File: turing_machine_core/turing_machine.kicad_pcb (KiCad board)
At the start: 2 copper layers, 127 parts, among them J1 Conn_02x07_Odd_Even, Q6 55NF06, U1 74LS14, U10 74LS193, U11 AS6C1008, U12 74LS193, U13 74LS374, U14 NE555P, U15 74LS03, U16 74LS74, U17 NE555P, U19 74LS139, U2 74LS00, U20 74LS74, U21 NE555P, U22 74LS245, U23 74LS245, U24 74LS245, U25 74LS245, U26 74LS245, U27 74LS245, U28 74LS245, U29 SST39SF020, U3 74LS14, U30 74LS245, U31 74LS245, U36 74LS245, U37 D5631LA, U38 D5631LR, U4 AS6C1008, U5 74LS193, U6 74LS374, U7 74LS193, U8 74LS30, U9 AS6C1008

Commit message: PCB layout planning and further documantation work
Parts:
- removed A1: RaspberryPi_Pico, Module:RaspberryPi_Pico_Common_THT
- removed C19, C20, C21, C23, C24, C25, C26, C27: 100nF, Capacitor_THT:C_Disc_D3.8mm_W2.6mm_P2.50mm
- removed C22: 100nF, Capacitor_THT:C_Disc_D5.1mm_W3.2mm_P5.00mm
- removed D1: LED_OPERATE_R, LED_THT:LED_D5.0mm
- removed D10: LED_HEADER2, LED_THT:LED_D5.0mm
- removed D11: LED_HEADER3, LED_THT:LED_D5.0mm
- removed D12: LED_HEADER4, LED_THT:LED_D5.0mm
- removed D13: LED_HEADER5, LED_THT:LED_D5.0mm
- removed D14: LED_HEADER6, LED_THT:LED_D5.0mm
- removed D15: LED_HEADER7, LED_THT:LED_D5.0mm
- removed D16: LED_HEADER8, LED_THT:LED_D5.0mm
- removed D17: LED_HEADER9, LED_THT:LED_D5.0mm
- removed D18: LED_HEADER10, LED_THT:LED_D5.0mm
- removed D19: LED_HEADER11, LED_THT:LED_D5.0mm
- removed D2: LED_PROGRAM_R, LED_THT:LED_D5.0mm
- removed D20: LED_HEADER12, LED_THT:LED_D5.0mm
- removed D21: LED_HEADER13, LED_THT:LED_D5.0mm
- removed D22: LED_HEADER14, LED_THT:LED_D5.0mm
- removed D23: LED_HEADER15, LED_THT:LED_D5.0mm
- removed D3: LED_CLK_G, LED_THT:LED_D5.0mm
- removed D4: LED_SESR_STATE_G, LED_THT:LED_D5.0mm
- removed D5: LED_RESET_Y, LED_THT:LED_D5.0mm
- removed D6: LED_FINISH_STATE_Y, LED_THT:LED_D5.0mm
- removed D7: LED_POWER_R, LED_THT:LED_D5.0mm
- removed D8: LED_HEADER0, LED_THT:LED_D5.0mm
- removed D9: LED_HEADER1, LED_THT:LED_D5.0mm
- removed J1: Conn_02x07_Odd_Even, Connector_IDC:IDC-Header_2x07_P2.54mm_Horizontal
- removed Q6: 55NF06, Package_TO_SOT_THT:TO-220-3_Horizontal_TabDown
- removed R1, R2: 220Ω, Resistor_THT:R_Axial_DIN0207_L6.3mm_D2.5mm_P10.16mm_Horizontal
- removed R10, R19, R8: 10kΩ, Resistor_THT:R_Axial_DIN0207_L6.3mm_D2.5mm_P10.16mm_Horizontal
- removed R12, R18, R20, R3, R4, R5, R6, R7: 1kΩ, Resistor_THT:R_Axial_DIN0207_L6.3mm_D2.5mm_P10.16mm_Horizontal
- removed R21: 68Ω, Resistor_THT:R_Axial_DIN0207_L6.3mm_D2.5mm_P10.16mm_Horizontal
- removed R22, R23, R24, R25, R26, R27, R28, R29, R30, R31, R32, R33, R34, R35, R36, R37, R38, R39, R40, R41, R42, R43, R44: 330Ω, Resistor_THT:R_Axial_DIN0207_L6.3mm_D2.5mm_P10.16mm_Horizontal
- removed RN4: 1,5kΩ, Connector_PinSocket_2.54mm:PinSocket_1x08_P2.54mm_Vertical
- removed RN6: 680Ω, Connector_PinSocket_2.54mm:PinSocket_1x08_P2.54mm_Vertical
- removed the U14 at (-63.5, 101.5)
- removed the U16 at (-52.8, 113.2)
- removed the U17 at (-52.8, 101.5)
- removed U19: 74LS139, Package_DIP:DIP-16_W7.62mm
- removed U20: 74LS74, Package_DIP:DIP-14_W7.62mm
- removed U21: NE555P, Package_DIP:DIP-8_W7.62mm
- removed U26, U27, U28, U30, U31, U36: 74LS245, Package_DIP:DIP-20_W7.62mm
- removed U29: SST39SF020, Package_DIP:DIP-32_W15.24mm
- removed the U3 at (-45.5, 77.5)
- removed U37: D5631LA, Display_7Segment:DA56-11CGKWA
- removed U38: D5631LR, Display_7Segment:DA56-11CGKWA
- removed the U8 at (-34.7, 77.5)
- added C7: 100nF, Capacitor_THT:C_Disc_D3.8mm_W2.6mm_P2.50mm, F.Cu at (50.2, 101.6)
- added U13: 74LS74, Package_DIP:DIP-14_W7.62mm, F.Cu at (33.0, 33.0)
- added U6: 74LS30, Package_DIP:DIP-14_W7.62mm, F.Cu at (33.0, 101.6)
- C1, C14, C3: value 10nF -> 100nF; footprint Capacitor_THT:C_Disc_D5.1mm_W3.2mm_P5.00mm -> Capacitor_THT:C_Disc_D3.8mm_W2.6mm_P2.50mm
- C2: value 10µF -> 100nF; footprint Capacitor_THT:CP_Radial_D5.0mm_P2.00mm -> Capacitor_THT:C_Disc_D3.8mm_W2.6mm_P2.50mm
- C5: value 22nF -> 100nF; footprint Capacitor_THT:C_Disc_D5.1mm_W3.2mm_P5.00mm -> Capacitor_THT:C_Disc_D3.8mm_W2.6mm_P2.50mm
- U1: value 74LS14 -> 74LS04
- U10: renamed from U11; footprint Package_DIP:DIP-32_W15.24mm -> Package_DIP:DIP-32_W15.24mm_Socket
- U15: value 74LS03 -> 74LS245; footprint Package_DIP:DIP-14_W7.62mm -> Package_DIP:DIP-20_W7.62mm
- U3: renamed from U4; footprint Package_DIP:DIP-32_W15.24mm -> Package_DIP:DIP-32_W15.24mm_Socket
- U7: renamed from U9; footprint Package_DIP:DIP-32_W15.24mm -> Package_DIP:DIP-32_W15.24mm_Socket
- moved C18 337.5 mm to (165.1, 22.2), turned to 90 degrees
- moved C11 327.4 mm to (168.3, 99.1), turned to -90 degrees
- moved C14 316.6 mm to (147.3, 22.2), turned to 90 degrees
- moved RN3 308.9 mm to (167.6, 27.9), turned to -90 degrees
- moved C9 308.7 mm to (150.5, 99.1), turned to -90 degrees
- moved C16 301.4 mm to (129.5, 22.2), turned to 90 degrees
- moved C8 290.6 mm to (132.7, 99.1), turned to -90 degrees
- moved RN1 289.3 mm to (149.9, 27.9), turned to -90 degrees
- moved C17 286.6 mm to (111.8, 22.2), turned to 90 degrees
- moved C12 279.1 mm to (94.0, 22.2), turned to 90 degrees
- moved RN2 274.3 mm to (132.1, 27.9), turned to -90 degrees
- moved C15 273.6 mm to (114.9, 63.5), turned to -90 degrees
- moved U14 272.5 mm to (139.7, 25.4)
- moved U18 258.6 mm to (157.5, 25.4)
- moved U16 245.2 mm to (121.9, 25.4)
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- renumbered U12 to U11, U13 to U12, U22 to U14, U23 to U16, U24 to U17, U25 to U18, U6 to U4, U7 to U8, U10 to U9
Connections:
- net RPI_DATA_DIR renamed DDIR
- C1 pad 1: Net-(U14-CV) -> +5V
- C1 pad 2: COM_{1} -> GND
- C10 pad 1: LPS_{0} -> +5V
- C10 pad 2: COM_{1} -> GND
- C11 pad 1: LPS_{0} -> +5V
- C11 pad 2: COM_{1} -> GND
- C12 pad 1: LPS_{0} -> +5V
- C12 pad 2: COM_{1} -> GND
- C13 pad 1: LPS_{0} -> +5V
- C13 pad 2: COM_{1} -> GND
- C14 pad 1: Net-(U21-CV) -> +5V
- C14 pad 2: COM_{1} -> GND
- C15 pad 1: LPS_{0} -> +5V
- C15 pad 2: COM_{1} -> GND
- C16 pad 1: LPS_{0} -> +5V
- C16 pad 2: COM_{1} -> GND
- C17 pad 1: LPS_{0} -> +5V
- C17 pad 2: COM_{1} -> GND
- C18 pad 1: LPS_{0} -> +5V
- C18 pad 2: COM_{1} -> GND
- C2 pad 1: ACP_{1} -> +5V
- C2 pad 2: COM_{1} -> GND
- C3 pad 1: Net-(U17-CV) -> +5V
- C3 pad 2: COM_{1} -> GND
- C4 pad 1: Net-(C4-Pad1) -> +5V
- C4 pad 2: COM_{1} -> GND
- C5 pad 1: Net-(U17-THR) -> +5V
- C5 pad 2: COM_{1} -> GND
- C6 pad 1: Net-(C6-Pad1) -> +5V
- C6 pad 2: COM_{1} -> GND
- C8 pad 1: Net-(C8-Pad1) -> +5V
- C8 pad 2: COM_{1} -> GND
- C9 pad 1: LPS_{0} -> +5V
- C9 pad 2: COM_{1} -> GND
- RN1 pad 1: COM_{1} -> GND
- RN2 pad 1: COM_{1} -> GND
- RN3 pad 1: LPS_{0} -> +5V
- RN3 pad 8: DIR -> /Control signal buffers/QR_~{OE}
- RN3 pad 9: unconnected-(RN3-R8-Pad9) -> DIR
- U1 pad 1: Net-(C4-Pad1) -> Net-(U1-Pad1)
- U1 pad 10: /RaspberryPI and power/REPROGRAM -> Net-(U13A-C)
- U1 pad 11: Net-(C8-Pad1) -> Net-(U1-Pad11)
- U1 pad 12: /RESET -> ~{OPERATE}
- U1 pad 13: ~{RESET} -> ~{PROGRAM}
- U1 pad 14: LPS_{0} -> +5V
- U1 pad 2: /Clock and Execution State/MAN_CLK -> /HP_EN_CLK
- U1 pad 3: Net-(U1-Pad3) -> DIR
- U1 pad 5: ~{PROGRAM} -> HP_EN
- U1 pad 6: ~{OPERATE} -> SR_WR
- U1 pad 7: COM_{1} -> GND
- U1 pad 8: Net-(U1-Pad3) -> /RESET
- U1 pad 9: Net-(C6-Pad1) -> ~{RESET}
- U10 pad 16: COM_{1} -> GND
- U10 pad 2: LPS_{0} -> +5V
- U10 pad 22: COM_{1} -> GND
- U10 pad 30: LPS_{0} -> +5V
- U10 pad 31: LPS_{0} -> +5V
- U10 pad 32: LPS_{0} -> +5V
- U11 pad 1: LPS_{0} -> +5V
- U11 pad 10: LPS_{0} -> +5V
- U11 pad 11: LPS_{0} -> +5V
- U11 pad 15: LPS_{0} -> +5V
- U11 pad 16: LPS_{0} -> +5V
- U11 pad 8: COM_{1} -> GND
- U11 pad 9: LPS_{0} -> +5V
- U12 pad 1: COM_{1} -> GND
- U12 pad 10: COM_{1} -> GND
- U12 pad 20: LPS_{0} -> +5V
- U14 pad 10: COM_{1} -> GND
- U14 pad 2: RD_{0} -> D_{0}
- U14 pad 20: LPS_{0} -> +5V
- U14 pad 3: RD_{1} -> D_{1}
- U14 pad 4: RD_{2} -> D_{2}
- U14 pad 5: RD_{3} -> D_{3}
- U14 pad 6: RD_{4} -> D_{4}
- U14 pad 7: RD_{5} -> D_{5}
- U14 pad 8: RD_{6} -> D_{6}
- U14 pad 9: RD_{7} -> D_{7}
- U15 pad 1: Net-(U1-Pad3) -> +5V
- U15 pad 10: /Clock and Execution State/COMBINED_CLK -> GND
- U15 pad 11: CLK -> D_{7}
- U15 pad 12: RPI_CLK -> D_{6}
- U15 pad 13: ~{OPERATE} -> D_{5}
- U15 pad 14: LPS_{0} -> D_{4}
- U15 pad 2: /Clock and Execution State/MAN_CLK -> QR_{0}
- U15 pad 3: /Clock and Execution State/COMBINED_CLK -> QR_{1}
- U15 pad 4: Net-(U1-Pad4) -> QR_{2}
- U15 pad 5: /Clock and Execution State/AUTO_CLK -> QR_{3}
- U15 pad 6: /Clock and Execution State/COMBINED_CLK -> QR_{4}
- U15 pad 7: COM_{1} -> QR_{5}
- U15 pad 8: CLK -> QR_{6}
- U15 pad 9: ~{PROGRAM} -> QR_{7}
- U16 pad 10: COM_{1} -> GND
- U16 pad 2: RD_{0} -> D_{0}
- U16 pad 20: LPS_{0} -> +5V
- U16 pad 3: RD_{1} -> D_{1}
- U16 pad 4: RD_{2} -> D_{2}
- U16 pad 5: RD_{3} -> D_{3}
- U16 pad 6: RD_{4} -> D_{4}
- U16 pad 7: RD_{5} -> D_{5}
- U16 pad 8: RD_{6} -> D_{6}
- U16 pad 9: RD_{7} -> D_{7}
- U17 pad 1: LPS_{0} -> +5V
- U17 pad 10: COM_{1} -> GND
- U17 pad 2: SESR_STATE -> HP_EN
- U17 pad 20: LPS_{0} -> +5V
- U17 pad 7: COM_{1} -> GND
- U17 pad 8: COM_{1} -> GND
- U17 pad 9: COM_{1} -> GND
- U18 pad 1: LPS_{0} -> +5V
- U18 pad 10: COM_{1} -> GND
- U18 pad 12: unconnected-(U25-B6-Pad12) -> /Control signal buffers/QR_~{OE}
- U18 pad 2: RD_{8} -> T_~{OE}_E
- U18 pad 20: LPS_{0} -> +5V
- U18 pad 3: RD_{9} -> T_~{WE}_E
- U18 pad 4: RD_{10} -> SYT_~{OE}_E
- U18 pad 5: RD_{11} -> SYT_~{WE}_E
- U18 pad 6: RD_{12} -> STT_~{OE}_E
- U18 pad 7: RD_{13} -> STT_~{WE}_E
- U18 pad 8: RD_{14} -> QR_~{OE}_E
- U18 pad 9: RD_{15} -> +5V
- U2 pad 1: CLK -> DIR
- U2 pad 10: /TI_EN_CLK -> HP_EN
- U2 pad 11: /DIR_DOWN -> Net-(U1-Pad11)
- U2 pad 12: /TI_EN_CLK -> ~{FINISH_STATE}
- U2 pad 13: Net-(U2-Pad13) -> CLK
- U2 pad 14: LPS_{0} -> +5V
- U2 pad 2: SESR_STATE -> /HP_EN_CLK
- U2 pad 3: Net-(U2-Pad3) -> /DIR_UP
- U2 pad 4: unconnected-(U2-Pad4) -> /HP_EN_CLK
- U2 pad 5: unconnected-(U2-Pad5) -> Net-(U1-Pad4)
- U2 pad 6: unconnected-(U2-Pad6) -> /DIR_DOWN
- U2 pad 7: COM_{1} -> GND
- U2 pad 8: /DIR_UP -> Net-(U1-Pad1)
- U2 pad 9: DIR -> CLK
- U3 pad 16: COM_{1} -> GND
- U3 pad 2: LPS_{0} -> +5V
- U3 pad 22: COM_{1} -> GND
- U3 pad 30: LPS_{0} -> +5V
- U3 pad 32: LPS_{0} -> +5V
- U4 pad 1: COM_{1} -> GND
- U4 pad 10: COM_{1} -> GND
- U4 pad 11: SESR_STATE -> HP_EN
- U4 pad 18: LPS_{0} -> +5V
- U4 pad 20: LPS_{0} -> +5V
- U5 pad 1: LPS_{0} -> +5V
- U5 pad 10: LPS_{0} -> +5V
- U5 pad 11: LPS_{0} -> +5V
- U5 pad 15: LPS_{0} -> +5V
- U5 pad 16: LPS_{0} -> +5V
- U5 pad 8: COM_{1} -> GND
- U5 pad 9: LPS_{0} -> +5V
- U7 pad 16: COM_{1} -> GND
- U7 pad 2: LPS_{0} -> +5V
- U7 pad 22: COM_{1} -> GND
- U7 pad 30: LPS_{0} -> +5V
- U7 pad 31: LPS_{0} -> +5V
- U7 pad 32: LPS_{0} -> +5V
- U8 pad 1: LPS_{0} -> +5V
- U8 pad 10: LPS_{0} -> +5V
- U8 pad 11: LPS_{0} -> +5V
- U8 pad 15: LPS_{0} -> +5V
- U8 pad 16: LPS_{0} -> +5V
- U8 pad 8: COM_{1} -> GND
- U8 pad 9: LPS_{0} -> +5V
- U9 pad 1: LPS_{0} -> +5V
- U9 pad 10: LPS_{0} -> +5V
- U9 pad 11: LPS_{0} -> +5V
- U9 pad 15: LPS_{0} -> +5V
- U9 pad 16: LPS_{0} -> +5V
- U9 pad 8: COM_{1} -> GND
- U9 pad 9: LPS_{0} -> +5V
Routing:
- net GND: track 0.00 -> 998.5 mm, vias 0 -> 16
- net +5V: track 0.00 -> 610.9 mm, vias 0 -> 2
- net QR_{1}: track 0.00 -> 226.9 mm, vias 0 -> 8
- net QR_{2}: track 0.00 -> 221.1 mm, vias 0 -> 8
- net QR_{0}: track 0.00 -> 215.5 mm, vias 0 -> 6
- net QR_{3}: track 0.00 -> 213.9 mm, vias 0 -> 8
- net S_{0}: track 0.00 -> 195.9 mm, vias 0 -> 3
- net S_{1}: track 0.00 -> 192.8 mm, vias 0 -> 4
- net S_{2}: track 0.00 -> 192.0 mm, vias 0 -> 4
- net QR_{6}: track 0.00 -> 187.6 mm, vias 0 -> 6
- net QR_{5}: track 0.00 -> 185.1 mm, vias 0 -> 7
- net QR_{4}: track 0.00 -> 180.3 mm, vias 0 -> 6
- net QR_{7}: track 0.00 -> 175.6 mm, vias 0 -> 3
- net S_{4}: track 0.00 -> 158.2 mm, vias 0 -> 6
- net S_{3}: track 0.00 -> 158.2 mm, vias 0 -> 4
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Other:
- board outline added: 152.4 x 110.5 mm
- board text added: "(STATE REGISTER)"
- board text added: "(STATE TRANSLATOR)"
- board text added: "(SYMBOL REGISTER)"
- board text added: "(SYMBOL TRANSLATOR)"
- board text added: "(TAPE)"
- board text added: "1"
- board text added: "2"
- board text added: "3"
- board text added: "4"
- board text added: "5"
- board text added: "6"
- board text added: "7"
- board text added: "8"
- board text added: "A"
- board text added: "B"
- board text added: "C"

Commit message: finished PCB planning
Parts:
- added D1: Power LED, LED_THT:LED_D5.0mm, F.Cu at (55.9, 21.6)
- added R1: 1kΩ, Resistor_THT:R_Axial_DIN0207_L6.3mm_D2.5mm_P10.16mm_Horizontal, F.Cu at (41.9, 21.6)
- added REF**: KiCad-Logo2_8mm_SilkScreen, Symbol:KiCad-Logo2_8mm_SilkScreen, B.Cu at (137.8, 59.7)
- added REF**: OSHW-Logo_11.4x12mm_SilkScreen, Symbol:OSHW-Logo_11.4x12mm_SilkScreen, B.Cu at (157.5, 59.7)
- moved C2 4.50 mm to (61.6, 33.0)
- moved C1 4.49 mm to (79.4, 33.0)
- moved C13 4.49 mm to (43.8, 33.0)
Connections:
- U13 pad 10: unconnected-(U13B-~{S}-Pad10) -> +5V
- U13 pad 11: unconnected-(U13B-C-Pad11) -> GND
- U13 pad 12: unconnected-(U13B-D-Pad12) -> GND
- U13 pad 13: unconnected-(U13B-~{R}-Pad13) -> GND
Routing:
- net STT_~{OE}: track 2.54 -> 277.3 mm, vias 0 -> 6
- net SYT_~{OE}: track 2.54 -> 253.7 mm, vias 0 -> 11
- net DIR_B: track 2.54 -> 224.3 mm, vias 0 -> 10
- net SYT_~{WE}: track 2.54 -> 177.0 mm, vias 0 -> 4
- net HP_EN: track 0.00 -> 166.3 mm, vias 0 -> 7
- net STT_~{WE}: track 2.54 -> 166.2 mm, vias 0 -> 2
- net DIR: track 0.00 -> 161.0 mm, vias 0 -> 9
- net Q_{0}: track 2.54 -> 146.6 mm, vias 0 -> 3
- net Q_{1}: track 2.54 -> 142.6 mm, vias 0 -> 4
- net T_~{OE}: track 2.54 -> 132.4 mm, vias 0 -> 6
- net Q_{2}: track 2.54 -> 130.8 mm, vias 0 -> 4
- net T_~{WE}: track 2.54 -> 129.5 mm, vias 0 -> 7
- net Q_{7}: track 2.54 -> 117.4 mm, vias 0 -> 3
- net Q_{6}: track 2.54 -> 116.3 mm, vias 0 -> 4
- net Q_{3}: track 2.54 -> 110.2 mm, vias 0 -> 4
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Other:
- board text added: "02.2026"
- board text added: "Fizyczna implementacja maszyny Turinga"
- board text added: "Paweł Szymańki"
- board text added: "Paweł Szymański 02.2026"
- board text added: "Power"
- board text added: "Tura"

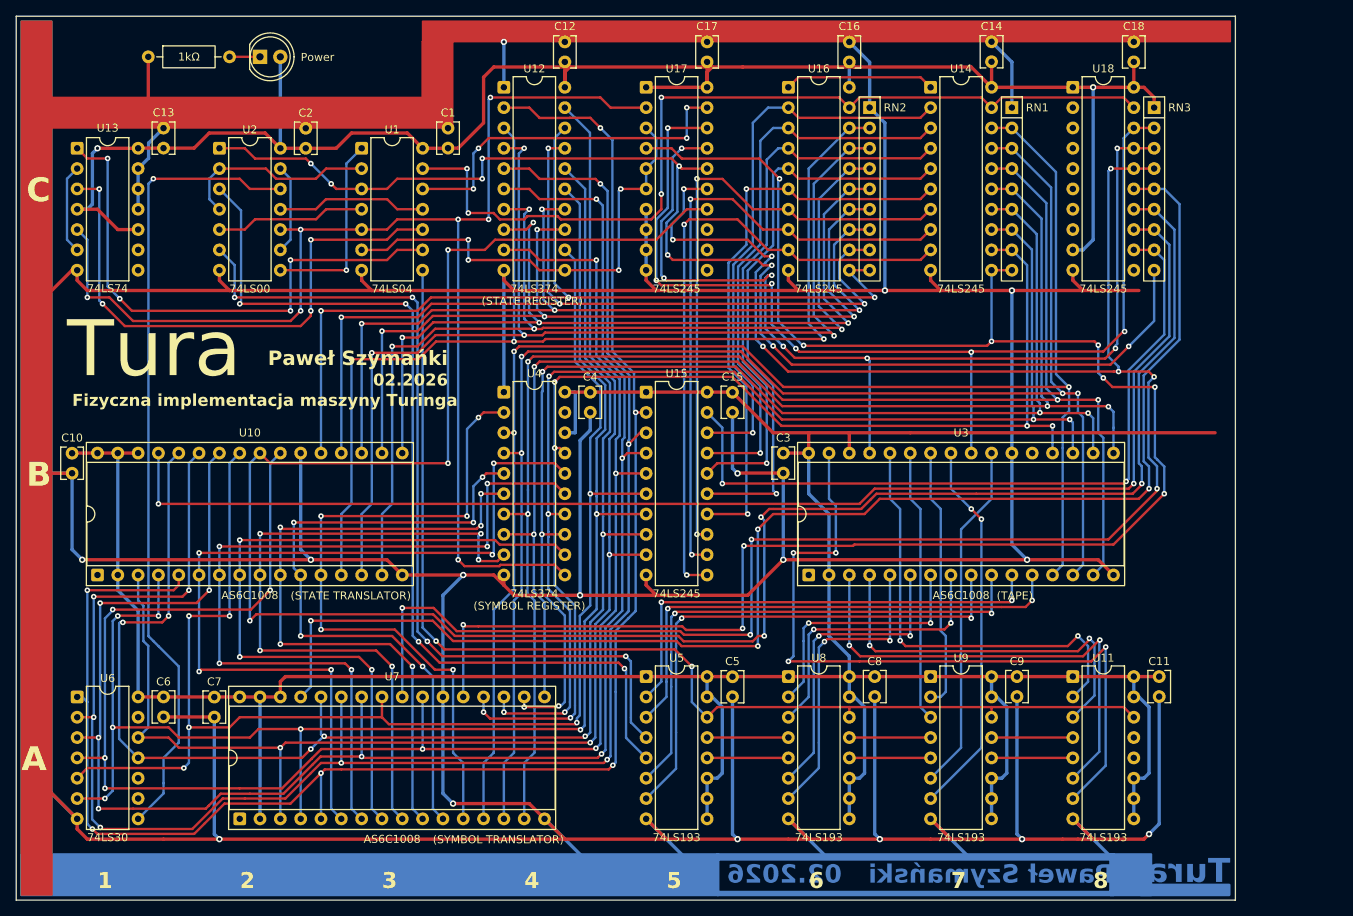
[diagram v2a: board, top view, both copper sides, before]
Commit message: adjusted PCB design for schematic fixes
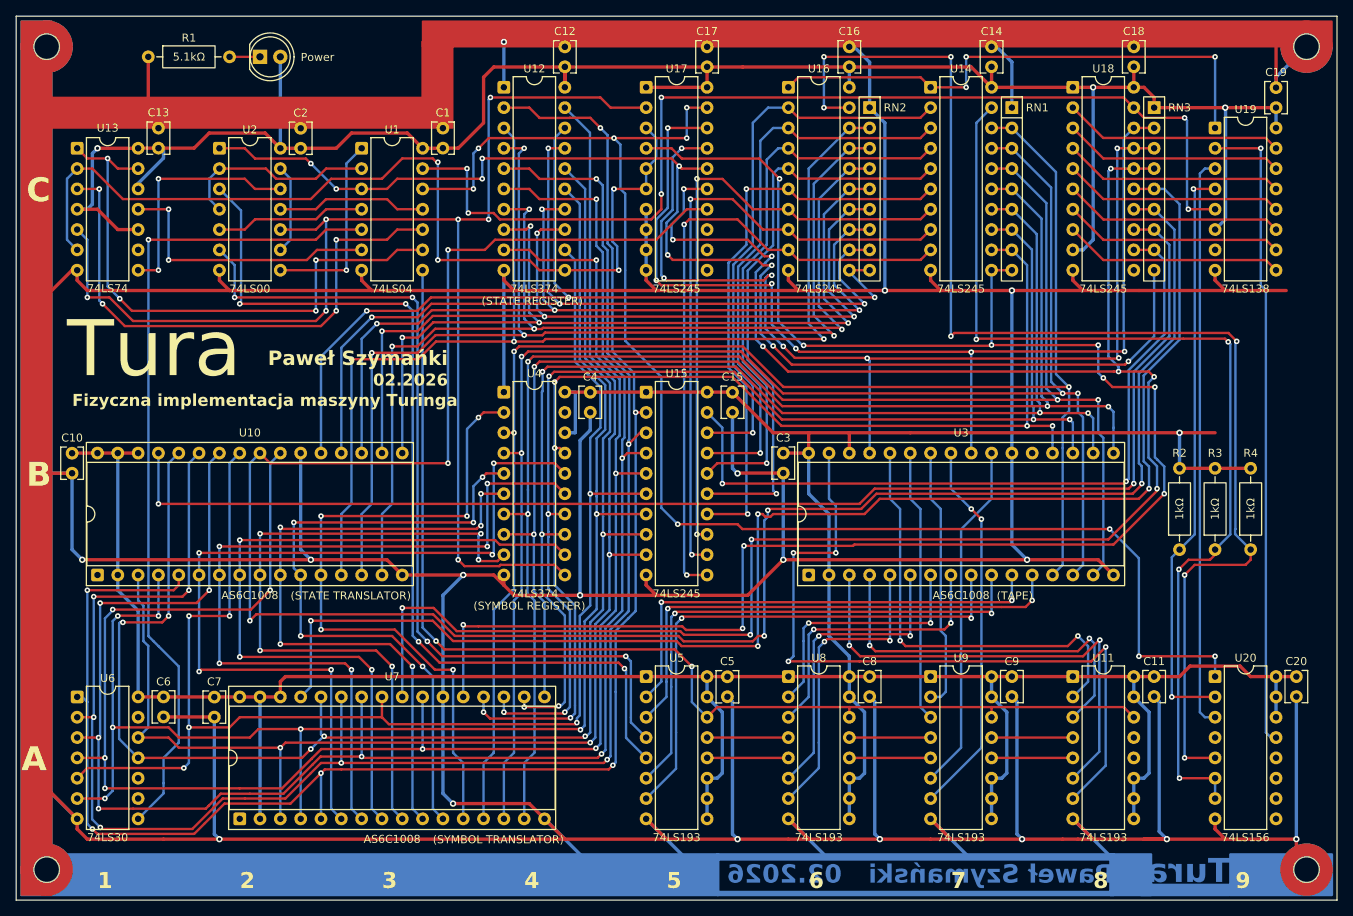
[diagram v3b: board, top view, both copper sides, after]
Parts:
- removed the REF** at (137.8, 59.7)
- removed the REF** at (157.5, 59.7)
- added C19: 100nF, Capacitor_THT:C_Disc_D3.8mm_W2.6mm_P2.50mm, F.Cu at (182.9, 27.9)
- added C20: 100nF, Capacitor_THT:C_Disc_D3.8mm_W2.6mm_P2.50mm, F.Cu at (185.4, 99.1)
- added R2: 1kΩ, Resistor_THT:R_Axial_DIN0207_L6.3mm_D2.5mm_P10.16mm_Horizontal, F.Cu at (170.8, 83.2)
- added R3: 1kΩ, Resistor_THT:R_Axial_DIN0207_L6.3mm_D2.5mm_P10.16mm_Horizontal, F.Cu at (175.3, 83.2)
- added R4: 1kΩ, Resistor_THT:R_Axial_DIN0207_L6.3mm_D2.5mm_P10.16mm_Horizontal, F.Cu at (179.7, 83.2)
- added REF**: MountingHole_3.2mm_M3, MountingHole:MountingHole_3.2mm_M3, F.Cu at (29.2, 123.2)
- added REF**: MountingHole_3.2mm_M3, MountingHole:MountingHole_3.2mm_M3, F.Cu at (186.7, 123.2)
- added REF**: MountingHole_3.2mm_M3, MountingHole:MountingHole_3.2mm_M3, F.Cu at (186.7, 20.3)
- added REF**: MountingHole_3.2mm_M3, MountingHole:MountingHole_3.2mm_M3, F.Cu at (29.2, 20.3)
- added U19: 74LS138, Package_DIP:DIP-16_W7.62mm, F.Cu at (175.3, 30.5)
- added U20: 74LS156, Package_DIP:DIP-16_W7.62mm, F.Cu at (175.3, 99.1)
- R1: value 1kΩ -> 5.1kΩ
- moved C11 0.64 mm to (167.6, 99.1)
- moved C1 0.64 mm to (78.7, 33.0)
- moved C5 0.64 mm to (114.3, 99.1)
- moved C14 0.64 mm to (147.3, 22.8)
- moved C13 0.63 mm to (43.2, 33.0)
- moved C2 0.63 mm to (61.0, 33.0)
- moved C8 0.63 mm to (132.1, 99.1)
- moved C9 0.63 mm to (149.9, 99.1)
- moved C12 0.61 mm to (94.0, 22.8)
- moved C16 0.61 mm to (129.5, 22.8)
- moved C17 0.61 mm to (111.8, 22.8)
- moved C18 0.61 mm to (165.1, 22.8)
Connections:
- U1 pad 5: HP_EN -> ~{FINISH_STATE}
- U1 pad 6: SR_WR -> Net-(U13B-C)
- U13 pad 11: GND -> Net-(U13B-C)
- U13 pad 12: GND -> +5V
- U13 pad 13: GND -> ~{RESET}
- U13 pad 2: Net-(U13A-D) -> SR_WR
- U13 pad 6: Net-(U13A-D) -> SR_WR
- U13 pad 8: unconnected-(U13B-~{Q}-Pad8) -> /Execution State & Power/CLK_EN
- U14 pad 19: ~{PROGRAM} -> ~{SYMB_BUF}
- U16 pad 19: ~{PROGRAM} -> ~{STAT_BUF}
- U2 pad 12: ~{FINISH_STATE} -> /Execution State & Power/CLK_EN
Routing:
- net ~{STAT_BUF}: track 0.00 -> 160.6 mm, vias 0 -> 7
- net ~{OPERATE}: track 44.6 -> 179.9 mm, vias 4 -> 9
- net ~{SYMB_BUF}: track 0.00 -> 127.4 mm, vias 0 -> 4
- net CS_{0}: track 0.00 -> 80.5 mm, vias 0 -> 1
- net ~{DT}: track 0.00 -> 72.9 mm, vias 0 -> 2
- net CS_{1}: track 0.00 -> 71.6 mm
- net +5V: track 622.5 -> 693.9 mm, vias 2 -> 4
- net GND: track 1009.7 -> 1076.7 mm, vias 16 -> 17
- net SR_WR: track 57.8 -> 118.9 mm
- net DDIR: track 18.8 -> 67.1 mm, vias 0 -> 3
- net Net-(U13B-C): track 0.00 -> 34.8 mm, vias 0 -> 2
- net /Execution State & Power/CLK_EN: track 0.00 -> 29.7 mm, vias 0 -> 2
- net T_~{WE}_E: track 0.00 -> 27.5 mm
- net T_~{OE}_E: track 0.00 -> 27.5 mm
- net SYT_~{WE}_E: track 0.00 -> 27.5 mm
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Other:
- board size 152.4 x 110.5 mm -> 165.1 x 110.5 mm
- board text added: "9"

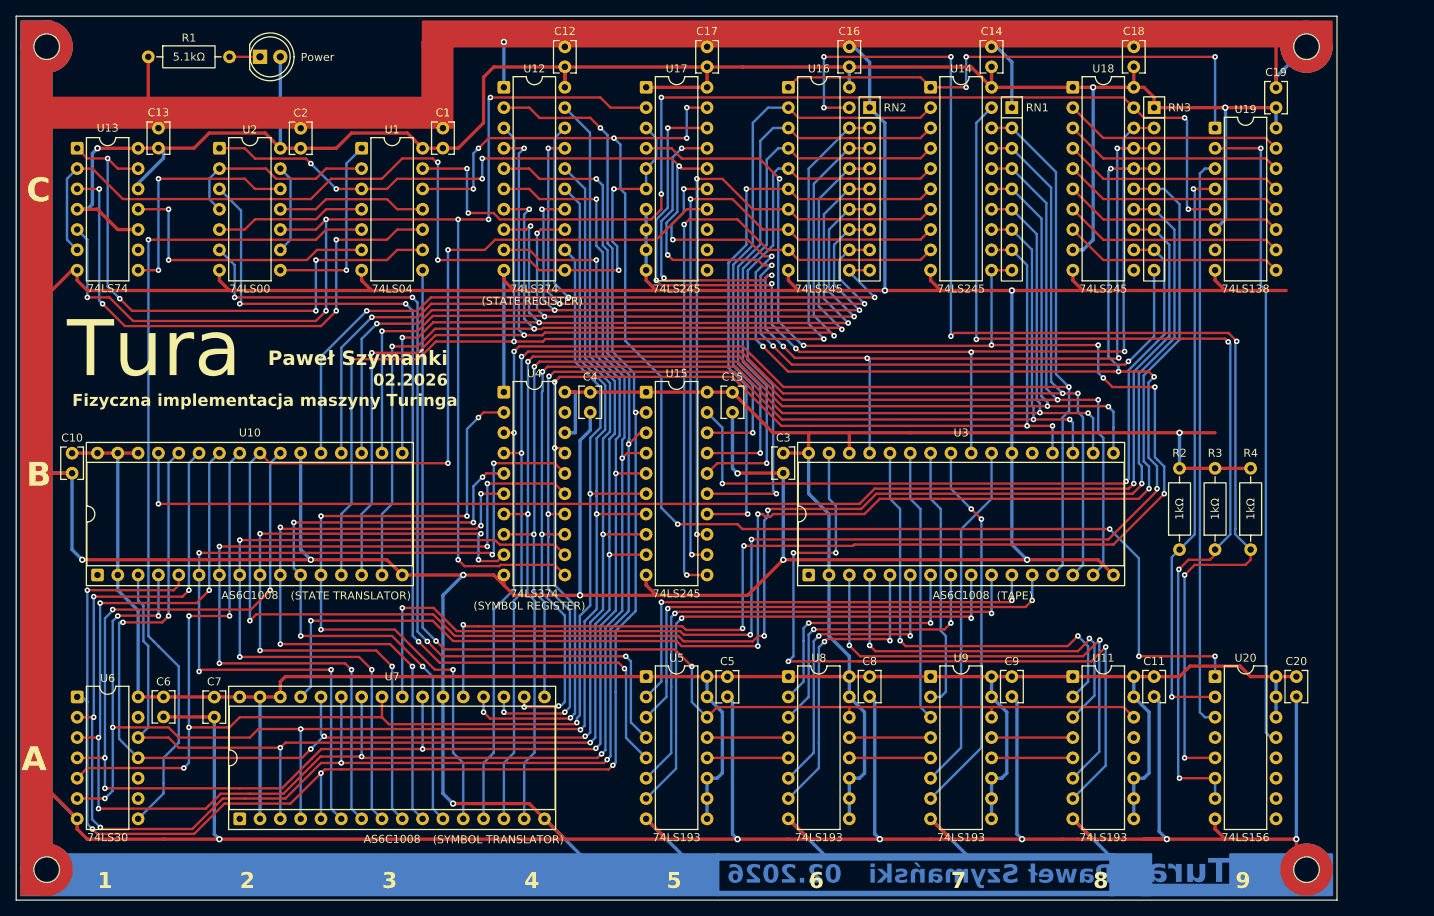
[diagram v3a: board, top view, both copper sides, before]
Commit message: added edge connector to PCB
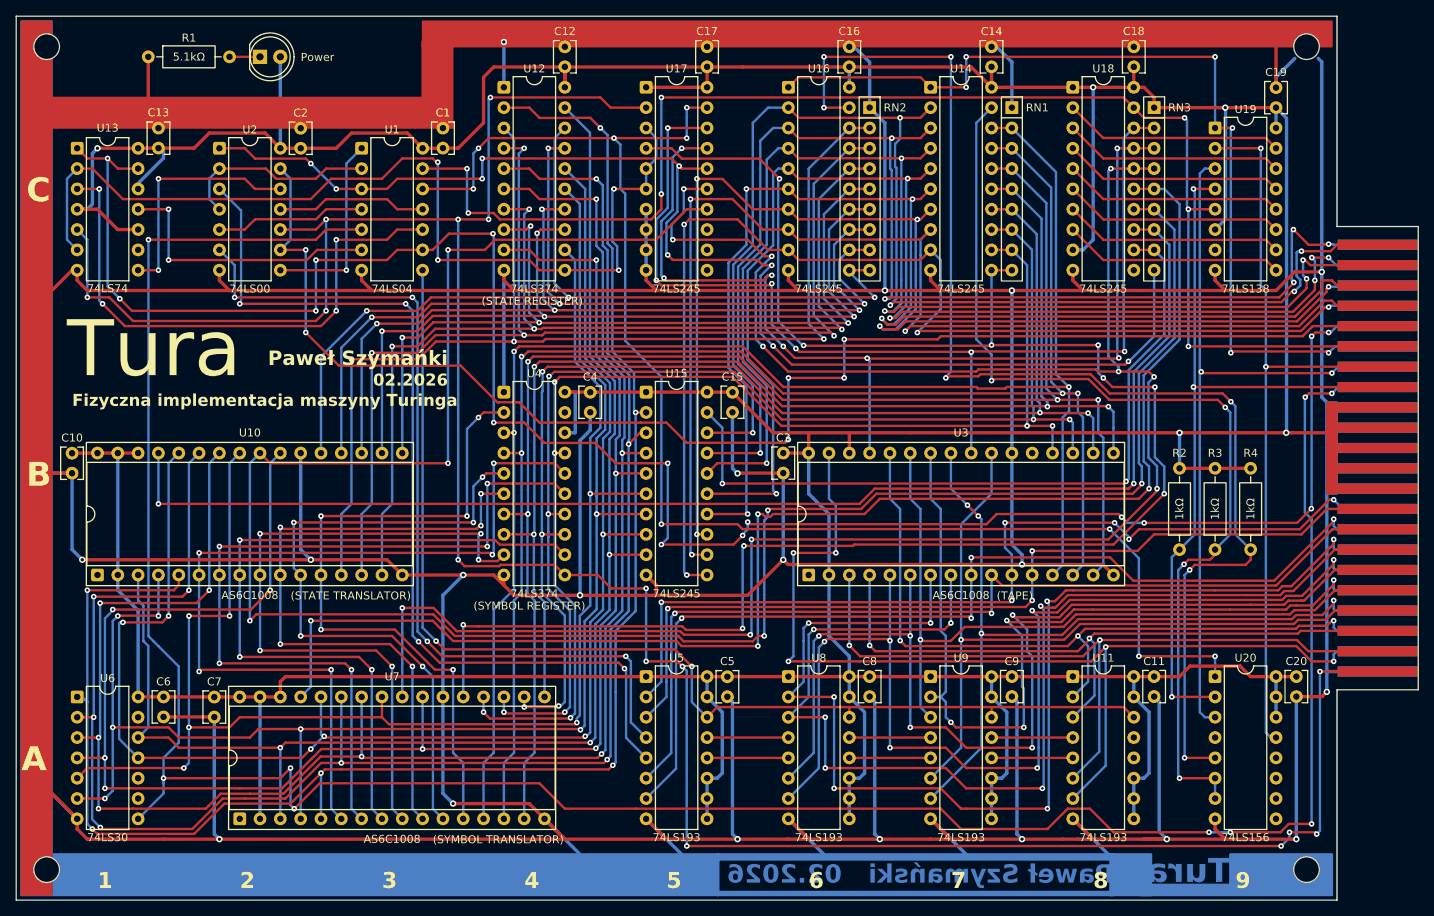
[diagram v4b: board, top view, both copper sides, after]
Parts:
- added J1: External Interface, Connector_Edge:Connector_Edge_2x22pin_odd, F.Cu at (195.6, 45.1)
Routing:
- net ~{FINISH_STATE}: track 103.2 -> 321.8 mm, vias 1 -> 9
- net ~{RESET}: track 72.2 -> 255.1 mm, vias 4 -> 15
- net CLK: track 11.2 -> 177.8 mm, vias 0 -> 6
- net HP_EN: track 170.7 -> 325.8 mm, vias 7 -> 15
- net H_{5}: track 31.5 -> 148.5 mm, vias 2 -> 7
- net H_{4}: track 35.8 -> 143.1 mm, vias 2 -> 6
- net H_{7}: track 38.1 -> 138.5 mm, vias 2 -> 6
- net H_{6}: track 38.7 -> 132.2 mm, vias 2 -> 5
- net GND: track 1076.7 -> 1170.0 mm, vias 17 -> 19
- net D_{1}: track 71.0 -> 162.4 mm, vias 1 -> 6
- net D_{0}: track 70.5 -> 161.8 mm, vias 1 -> 5
- net D_{2}: track 70.5 -> 158.7 mm, vias 1 -> 5
- net D_{3}: track 72.5 -> 158.8 mm, vias 1 -> 6
- net D_{4}: track 71.7 -> 155.8 mm, vias 2 -> 4
- net D_{5}: track 77.5 -> 159.9 mm, vias 2 -> 5
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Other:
- outline, holes or cut-outs redrawn

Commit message: small border ground plane adjustments and added backside logos
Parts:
- added REF**: OSHW-Logo_11.4x12mm_SilkScreen, Symbol:OSHW-Logo_11.4x12mm_SilkScreen, B.Cu at (168.3, 59.7)
- added REF**: KiCad-Logo2_8mm_SilkScreen, Symbol:KiCad-Logo2_8mm_SilkScreen, B.Cu at (137.8, 59.1)
- added REF**: OSHW-Logo_19x20mm_SilkScreen, Symbol:OSHW-Logo_19x20mm_SilkScreen, B.Cu at (226.1, 45.1)
- added REF**: KiCad-Logo2_12mm_SilkScreen, Symbol:KiCad-Logo2_12mm_SilkScreen, B.Cu at (226.1, 64.1)
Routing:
- net GND: track 1170.0 -> 1194.1 mm
